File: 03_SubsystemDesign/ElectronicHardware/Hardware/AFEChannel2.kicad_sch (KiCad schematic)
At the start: 30 parts, among them U2101 OPA690xDBV, U2102 AD8139

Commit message: pcb design work in progress
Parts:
- removed C2101, C2102, C2103, C2104, C2105, C2106, C2107, C2108, C2109, C2110, C2111, C2112, C2113, C2114, C2115, C2116, C2117: C, Capacitor_SMD:C_0805_2012Metric, symbol Device:C
- removed D2101: D_SiPM, symbol Device:D_SiPM
- removed R2101: R, Resistor_SMD:R_0805_2012Metric, symbol Device:R
- removed RN2101, RN2102, RN2103, RN2104: R_Pack04, Resistor_SMD:R_Array_Convex_4x0612, symbol Device:R_Pack04
- removed TP2101, TP2102, TP2103, TP2104, TP2105: TestPoint, TestPoint:TestPoint_Pad_D1.0mm, symbol Connector:TestPoint
- removed U2101: OPA690xDBV, Package_TO_SOT_SMD:SOT-23-6, symbol Amplifier_Operational:OPA690xDBV
- removed U2102: AD8139, Package_SO:SOIC-8_5.3x5.3mm_P1.27mm, symbol GammaSpectrometer:AD8139
- added C510, C511, C514, C516, C517, C518: C, Capacitor_SMD:C_0805_2012Metric, symbol Device:C
- added C512: 2n2, Capacitor_SMD:C_0805_2012Metric, symbol Device:C
- added C513, C526: 1u, Capacitor_SMD:C_0805_2012Metric, symbol Device:C
- added C515, C527: 100n, Capacitor_SMD:C_0805_2012Metric, symbol Device:C
- added C521: 150p, Capacitor_SMD:C_0805_2012Metric, symbol Device:C
- added C522, C523, C524: 100p, Capacitor_SMD:C_0805_2012Metric, symbol Device:C
- added C525, C528: 10n, Capacitor_SMD:C_0805_2012Metric, symbol Device:C
- added D502, D503: D_SiPM, symbol Device:D_SiPM
- added R508: 2k, Resistor_SMD:R_0805_2012Metric, symbol Device:R
- added RN501: 1k, Resistor_SMD:R_Array_Convex_4x0612, symbol Device:R_Pack04
- added RN502: 620R, Resistor_SMD:R_Array_Convex_4x0612, symbol Device:R_Pack04
- added RN503, RN504: 100R, Resistor_SMD:R_Array_Convex_4x0612, symbol Device:R_Pack04
- added TP503, TP504, TP505, TP506, TP507: TestPoint, TestPoint:TestPoint_Pad_D1.0mm, symbol Connector:TestPoint
- added U502: LTC6268xS6-10, Package_TO_SOT_SMD:TSOT-23-6, symbol Amplifier_Operational:LTC6268xS6-10
- added U503: AD8139, Package_SO:SOIC-8_5.3x5.3mm_P1.27mm, symbol GammaSpectrometer:AD8139
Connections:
- net AFE_OUT_N: now also C522.1, C523.2, RN504.3 (R3.1), RN504.4 (R4.1), TP506.1
- net AFE_OUT_P: now also C523.1, C524.2, RN504.1 (R1.1), RN504.2 (R2.1), TP507.1
- net GND: now also C510.2, C511.2, C513.2, C514.2, C515.2, C516.2, C522.2, C524.1, C525.2, C526.2, C527.2, C528.2, RN501.3 (R3.1), RN501.4 (R4.1), U502.2 (V-), U503.6 (V-)
- net SIPM_BIAS: now also D502.1 (K), D503.1 (K)
- new net: C521.1, RN503.1 (R1.1), RN503.2 (R2.1), RN504.7 (R2.2), RN504.8 (R1.2), TP505.1
- new net: C521.2, RN503.3 (R3.1), RN503.4 (R4.1), RN504.5 (R4.2), RN504.6 (R3.2), TP504.1
- new net: C517.2, RN502.4 (R4.1), RN503.5 (R4.2), RN503.6 (R3.2), U503.5 (-)
- new net: C518.2, RN502.1 (R1.1), RN503.7 (R2.2), RN503.8 (R1.2), U503.4 (+)
- new net: C512.2, R508.1, RN501.1 (R1.1), RN501.2 (R2.1), TP503.1, U502.1
- new net: C512.1, D502.2 (A), D503.2 (A), R508.2, U502.4 (-)
- new net: C518.1, RN501.5 (R4.2), RN501.6 (R3.2), RN502.8 (R1.2), U503.1 (-)
- new net: C517.1, RN501.7 (R2.2), RN501.8 (R1.2), RN502.5 (R4.2), U503.8 (+)
- new net +5V0_A: C513.1, C515.1, C525.1, C526.1, C527.1, C528.1, U502.5 (~{SHDN}), U502.6 (V+), U503.3 (V+)
- new net 1V5_REF: C510.1, C511.1, C514.1, C516.1, U502.3 (+), U503.2 (VCM)
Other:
- note added: "Anti-Aliasing Filter (AAF)"
- note removed: "10-20 MHz Anti-Aliasing Filter (AAF) Value TBD"
- note removed: "75MHz protects stability of diff opamp from ADC's switched-cap input kickback TBD check if needed?"

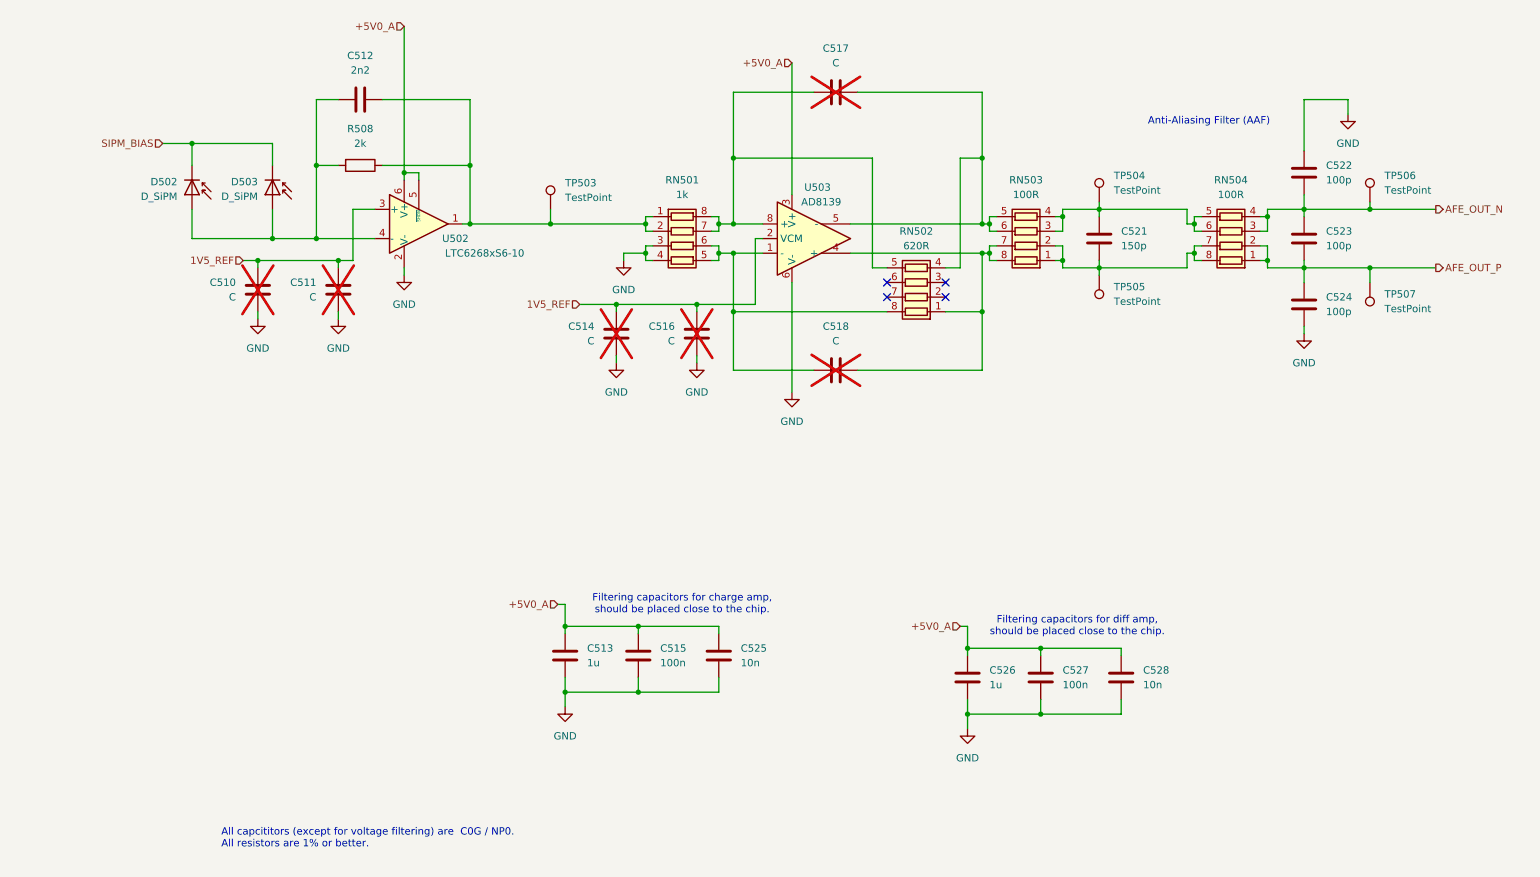
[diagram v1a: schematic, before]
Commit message: improve CAD folder structure and PCB
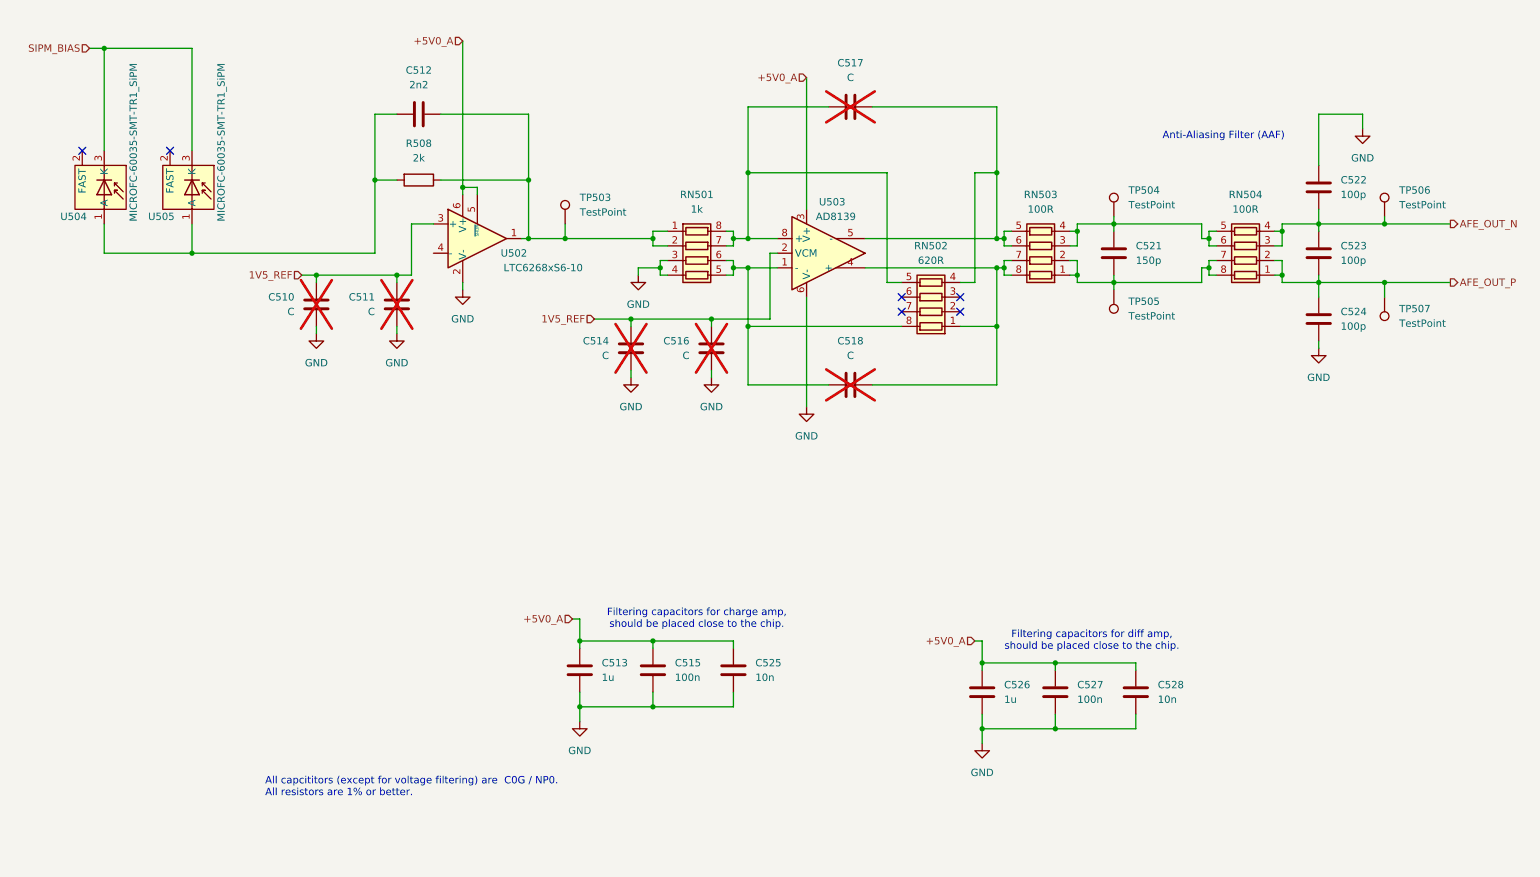
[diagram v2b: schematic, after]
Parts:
- removed D502, D503: D_SiPM, symbol Device:D_SiPM
- added U504, U505: MICROFC-60035-SMT-TR1_SiPM, GammaSpectrometer:MICROFC-60035-SMT-TR1_SiPM, symbol GammaSpectrometer:MICROFC-60035-SMT-TR1_SiPM
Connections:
- net SIPM_BIAS: now also U504.3 (K), U505.3 (K)
- net at C512.1, R508.2: now also U504.1 (A), U505.1 (A); no longer U502.4 (-)
- no-connect marks 4 -> 6
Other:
- moved on the sheet: C510, C511, C512, C513, C514, C515, C516, C517, C518, C521, C522, C523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
